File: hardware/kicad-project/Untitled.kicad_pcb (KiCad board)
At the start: 2 copper layers, 110 x 70 mm, 75 parts, among them CN2 ST-0322D00-071-1A2H, J8 Conn_01x50, Q1 DMG2301L-7, Q2 DMG2301L-7, Q3 DMG2301L-7, SW1 TS-1187A-B-A-B, SW10 TS-1135-C, SW2 TS-1187A-B-A-B, SW4 K2-1109SP-C4SA, SW5 K2-1109SP-C4SA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

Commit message: wip
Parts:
- removed R1, R11: 0, Resistor_SMD:R_0603_1608Metric
- added JP1: Gain jumper, Jumper:SolderJumper-2_P1.3mm_Open_Pad1.0x1.5mm, F.Cu at (95.7, 89.0)
- added JP2: Power jumper, Jumper:SolderJumper-2_P1.3mm_Open_Pad1.0x1.5mm, F.Cu at (140.7, 92.0)
- added TP1: Test OUTP, Connector_PinHeader_2.54mm:PinHeader_1x01_P2.54mm_Vertical, F.Cu at (108.6, 125.0)
- added TP2: Test OUTN, Connector_PinHeader_2.54mm:PinHeader_1x01_P2.54mm_Vertical, F.Cu at (105.0, 125.0)
- moved C15 0.18 mm to (185.1, 62.0)
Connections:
- C15 pad 1: Net-(Card1-VDD) -> GND
- Card1 pad 4: Net-(Card1-VDD) -> CONTROLLED_3.3V
- U1 pad 28: unconnected-(U1-IO35-Pad28) -> LCD_MOSI
- U1 pad 29: SD_DAT_1 -> LCD_DC
- U1 pad 30: SD_DAT_0 -> LCD_SCK
- U1 pad 31: SD_CLK -> LCD_CS
- U1 pad 32: SD_CMD -> SD_DAT_1
- U1 pad 33: SD_DAT_3 -> SD_DAT_0
- U1 pad 34: SD_DAT_2 -> SD_CLK
- U1 pad 35: unconnected-(U1-IO42-Pad35) -> SD_CMD
- U1 pad 38: unconnected-(U1-IO2-Pad38) -> SD_DAT_3
- U1 pad 39: unconnected-(U1-IO1-Pad39) -> SD_DAT_2
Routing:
- net LCD_CS: track 0.00 -> 55.0 mm, vias 0 -> 2
- net LCD_SCK: track 0.00 -> 53.9 mm, vias 0 -> 2
- net LCD_DC: track 0.00 -> 52.8 mm, vias 0 -> 2
- net LCD_MOSI: track 0.00 -> 51.7 mm, vias 0 -> 2
- net Net-(Card1-VDD): track 7.69 -> 0.00 mm
- net SD_DAT_3: track 94.2 -> 100.7 mm
- net SD_DAT_2: track 95.2 -> 101.4 mm
- net Net-(U6-OUTP): track 21.4 -> 26.8 mm
- net CONTROLLED_3.3V: track 187.5 -> 192.8 mm
- net +3.3V: track 149.5 -> 154.4 mm
- net SD_CLK: track 85.6 -> 90.3 mm
- net SD_CMD: track 89.2 -> 93.5 mm
- net SD_DAT_1: track 79.8 -> 83.8 mm
- net SD_DAT_0: track 80.3 -> 84.1 mm
- net GAIN_CONTROL: track 60.4 -> 57.0 mm, vias 4 -> 3
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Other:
- board text removed: "BETA"

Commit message: update MAX sdmode to 634k R
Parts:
- R8: value 1M -> 634k
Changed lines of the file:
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@@
         (effects (font (size 1 1) (thickness 0.15)))
     )
-    (fp_text value "1M" (at 3 6.43 90) (layer "F.Fab")
+    (fp_text value "634k" (at 3 6.43 90) (layer "F.Fab")
         (effects (font (size 1 1) (thickness 0.15)))
     )
@@
   (gr_circle (center 119.797921 117.336565) (end 128.297921 117.336565)
     (stroke (width 0.1) (type dash)) (fill none) (layer "F.SilkS"))
+  (gr_rect (start 139 91) (end 147 94)
+    (stroke (width 0.1524) (type default)) (fill none) (layer "F.SilkS"))
   (gr_line (start 134.313025 126.403429) (end 134.313025 105.55587)
     (stroke (width 0.2) (type solid)) (layer "Edge.Cuts"))

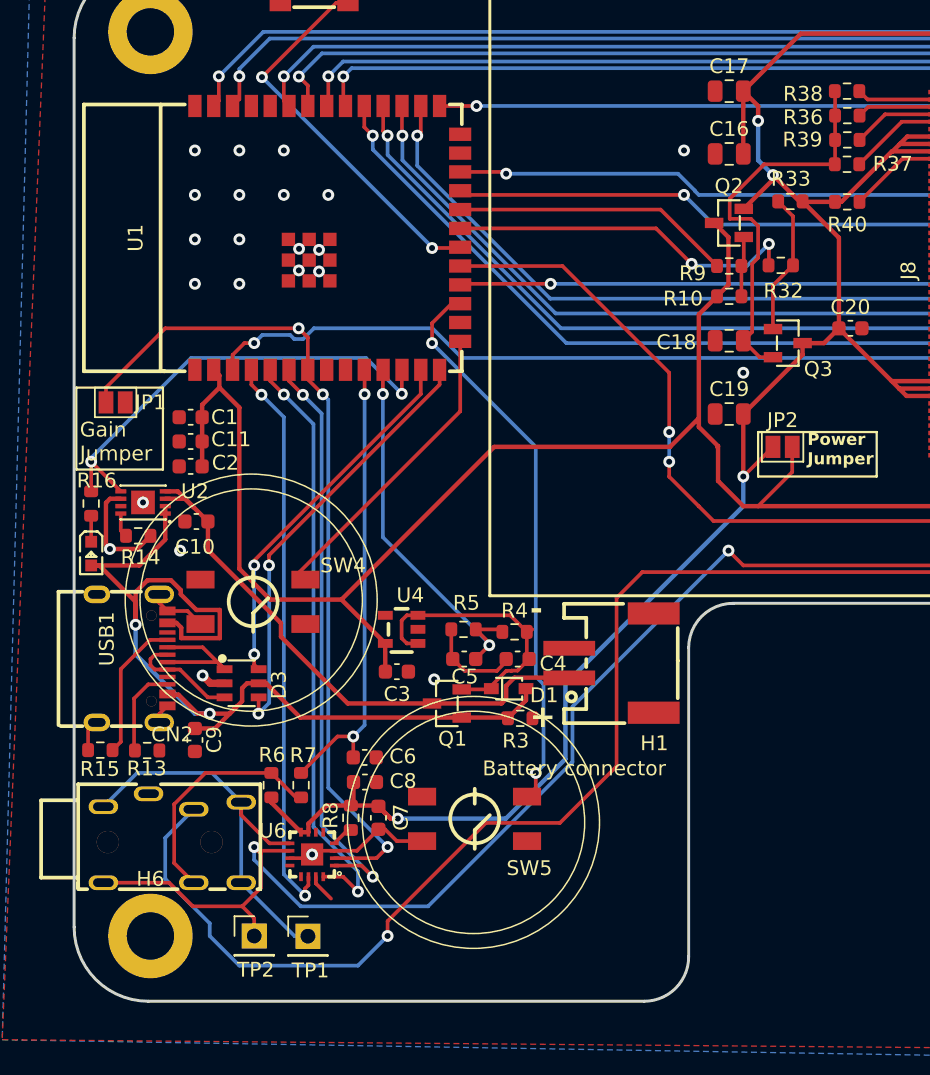
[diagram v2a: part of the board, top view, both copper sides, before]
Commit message: fix mosfet
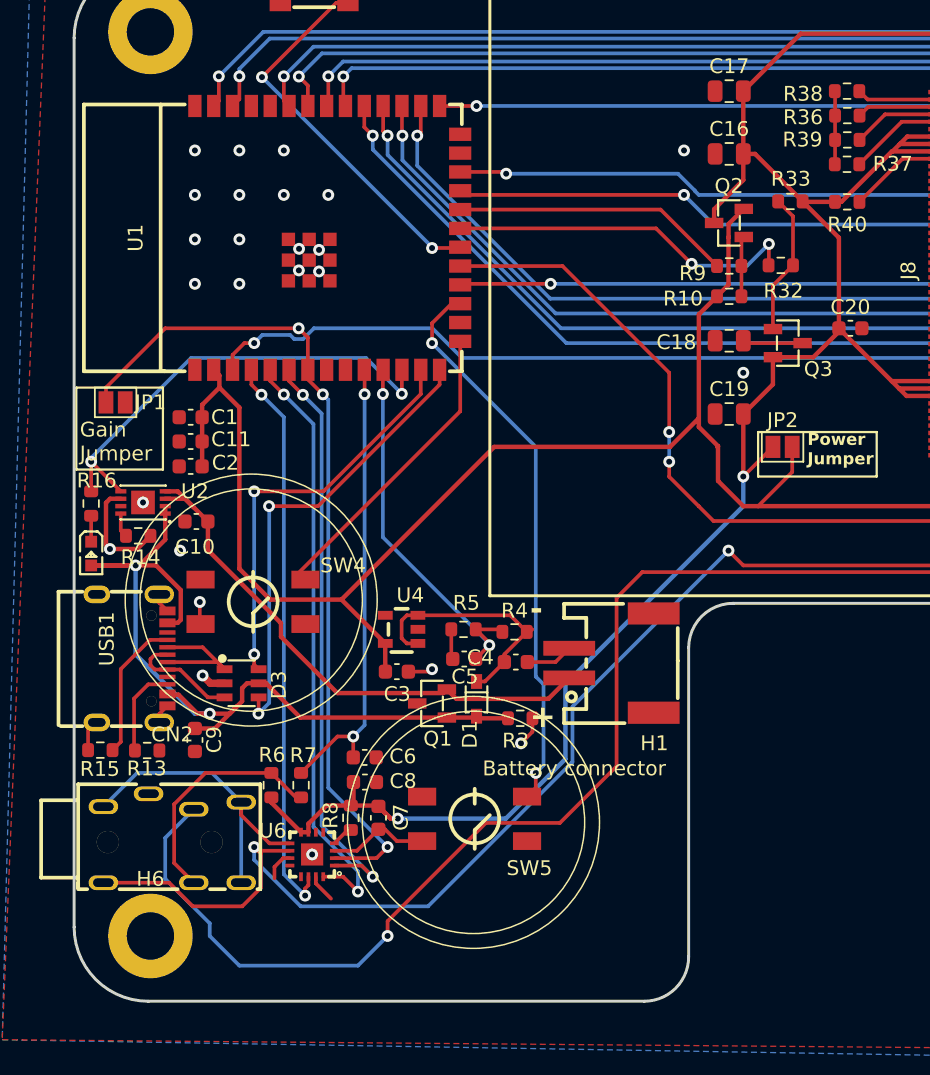
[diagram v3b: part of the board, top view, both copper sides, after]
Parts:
- removed TP1: Test OUTP, Connector_PinHeader_2.54mm:PinHeader_1x01_P2.54mm_Vertical
- removed TP2: Test OUTN, Connector_PinHeader_2.54mm:PinHeader_1x01_P2.54mm_Vertical
- moved D1 2.28 mm to (120.0, 109.0), turned to -90 degrees
- moved Q1 1.00 mm to (117.0, 109.3)
- moved C4 0.24 mm to (122.7, 106.5), turned to 180 degrees
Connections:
- C18 pad 2: Net-(Q3-S) -> Net-(Q3-D)
- Q1 pad 2: Net-(D1-K) -> +BATT
- Q1 pad 3: +BATT -> Net-(D1-K)
- Q2 pad 2: CONTROLLED_3.3V -> +3.3V
- Q2 pad 3: +3.3V -> CONTROLLED_3.3V
- Q3 pad 2: Net-(Q3-S) -> CONTROLLED_3.3V
- Q3 pad 3: CONTROLLED_3.3V -> Net-(Q3-D)
- R36 pad 2: Net-(Q3-S) -> Net-(Q3-D)
- R37 pad 2: Net-(Q3-S) -> Net-(Q3-D)
- R38 pad 2: Net-(Q3-S) -> Net-(Q3-D)
- R39 pad 2: Net-(Q3-S) -> Net-(Q3-D)
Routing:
- net Net-(Q3-S): track 27.1 -> 0.00 mm
- net +5V: track 70.3 -> 60.2 mm
- net Net-(Q3-D): track 0.00 -> 9.01 mm
- net Net-(U6-OUTP): track 26.8 -> 21.4 mm
- net GPIO_19: track 25.0 -> 27.7 mm
- net Net-(D1-K): track 19.1 -> 16.7 mm
- net Net-(U6-OUTN): track 101.3 -> 99.0 mm
- net GPIO_20: track 29.4 -> 31.3 mm
- net +3.3V: track 154.4 -> 155.4 mm
- net GND: track 62.0 -> 62.8 mm, vias 23 -> 25
- net CONTROLLED_3.3V: track 192.8 -> 192.0 mm, vias 4 -> 2
- net +BATT: track 38.4 -> 37.7 mm

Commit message: wip
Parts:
- moved H1 37.6 mm to (166.7, 107.0), turned to -90 degrees
- moved H2 37.4 mm to (129.2, 107.3), turned to 90 degrees
- moved R13 5.78 mm to (103.0, 110.0)
- moved C7 5.62 mm to (116.0, 122.0)
- moved R8 5.19 mm to (113.0, 122.0)
- moved C6 4.80 mm to (107.8, 114.0)
- moved C3 4.11 mm to (112.0, 104.0)
- moved U4 3.79 mm to (113.1, 101.0)
- moved R6 3.69 mm to (109.0, 117.2)
- moved C8 3.43 mm to (113.0, 118.0)
- moved C20 3.16 mm to (146.2, 87.0)
- moved Q3 3.16 mm to (144.0, 84.0)
- moved R9 2.88 mm to (134.2, 79.8)
- moved D3 2.85 mm to (107.0, 108.0)
- moved R7 2.62 mm to (107.0, 117.2)
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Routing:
- net Net-(CN2-Pad5): track 101.7 -> 30.3 mm, vias 1 -> 0
- net +BATT: track 37.7 -> 90.9 mm, vias 0 -> 2
- net Net-(U6-OUTN): track 99.0 -> 53.3 mm, vias 2 -> 0
- net GND: track 62.8 -> 32.0 mm, vias 25 -> 52
- net Net-(Q3-D): track 9.01 -> 28.8 mm, vias 0 -> 2
- net +5V: track 60.2 -> 41.9 mm, vias 2 -> 0
- net +3.3V: track 155.4 -> 140.3 mm, vias 0 -> 4
- net BTN_4: track 82.2 -> 91.6 mm
- net EN: track 123.9 -> 132.7 mm
- net BTN_5: track 26.1 -> 33.2 mm
- net BOOT: track 106.2 -> 112.5 mm
- net CONTROLLED_3.3V: track 192.0 -> 198.1 mm, vias 2 -> 8
- net LCD_CS: track 55.0 -> 61.0 mm
- net Net-(CN2-Pad6): track 16.0 -> 10.2 mm
- net I2S_DOUT: track 39.4 -> 44.6 mm
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
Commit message: wip
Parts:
- moved C7 7.73 mm to (109.7, 117.5), turned to 180 degrees
- moved C4 6.94 mm to (116.3, 102.0), turned to 90 degrees
- moved R6 4.37 mm to (112.0, 114.0), turned to 180 degrees
- moved C8 3.38 mm to (109.8, 119.0)
- moved C3 0.93 mm to (112.7, 103.4)
- moved C5 0.83 mm to (118.8, 105.0)
- moved R4 0.83 mm to (122.8, 104.0)
- moved R5 0.83 mm to (118.8, 102.0)
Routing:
- net Net-(CN2-Pad6): track 10.2 -> 13.4 mm
- net GND: track 32.0 -> 30.5 mm
- net Net-(D1-K): track 18.9 -> 17.8 mm
- net CONTROLLED_3.3V: track 198.1 -> 199.0 mm
- net +3.3V: track 140.3 -> 139.4 mm
- net BAT_READ: track 23.2 -> 24.0 mm

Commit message: wip
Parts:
- removed R36, R37, R38, R39: 10, Resistor_SMD:R_0603_1608Metric
- removed U4: XC6220B331MR, easyeda2kicad:SOT-23-5_L2.9-W1.6-P0.95-LS2.8-BR
- added C12: 10uf, Capacitor_SMD:C_0603_1608Metric, F.Cu at (110.7, 98.3)
- added R1: 10, Resistor_SMD:R_0603_1608Metric, F.Cu at (145.0, 66.0)
- added R11: 10, Resistor_SMD:R_0603_1608Metric, F.Cu at (145.0, 70.0)
- added R17: 10, Resistor_SMD:R_0603_1608Metric, F.Cu at (145.0, 72.0)
- added R2: 10, Resistor_SMD:R_0603_1608Metric, F.Cu at (145.0, 68.0)
- added U3: ME6217C33P5G, easyeda2kicad:SOT-89-5_L4.5-W2.5-P1.50-LS4.5-BR, F.Cu at (113.5, 101.3)
- C4: value 10uF -> 10uf
- moved C5 16.4 mm to (112.9, 89.7)
- moved C3 6.82 mm to (117.9, 99.0), turned to -90 degrees
- moved C4 3.09 mm to (116.3, 98.9), turned to -90 degrees
- moved R5 2.00 mm to (118.8, 104.0)
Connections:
- net /random/LCD_NRST renamed Net-(J8-Pin_10)
- C18 pad 2: Net-(Q3-D) -> Net-(J8-Pin_1)
- C3 pad 1: +3.3V -> GND
- C3 pad 2: GND -> Net-(D1-K)
- J8 pad 1: GND -> Net-(J8-Pin_1)
- J8 pad 7: CONTROLLED_3.3V -> +3.3V
- J8 pad 8: CONTROLLED_3.3V -> +3.3V
- J8 pad 9: CONTROLLED_3.3V -> +3.3V
- Q3 pad 2: CONTROLLED_3.3V -> +3.3V
- Q3 pad 3: Net-(Q3-D) -> Net-(J8-Pin_1)
- R33 pad 2: CONTROLLED_3.3V -> +3.3V
- R40 pad 1: CONTROLLED_3.3V -> +3.3V
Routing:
- net Net-(Q3-D): track 28.8 -> 0.00 mm, vias 2 -> 0
- net Net-(D1-K): track 17.8 -> 34.2 mm
- net Net-(J8-Pin_1): track 0.00 -> 10.4 mm, vias 0 -> 2
- net GPIO_20: track 27.8 -> 32.2 mm
- net +3.3V: track 139.4 -> 136.4 mm
- net BAT_READ: track 24.0 -> 22.0 mm
- net GND: track 30.5 -> 29.9 mm, vias 52 -> 28
- net +BATT: track 90.9 -> 91.6 mm

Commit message: wip
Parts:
- removed JP1: Gain jumper, Jumper:SolderJumper-2_P1.3mm_Open_Pad1.0x1.5mm
- removed JP2: Power jumper, Jumper:SolderJumper-2_P1.3mm_Open_Pad1.0x1.5mm
- removed Q2: DMG2301L-7, easyeda2kicad:SOT-23-3_L2.9-W1.3-P1.90-LS2.4-BR
- removed R10: 100k, Resistor_SMD:R_0603_1608Metric
- removed R8: 634k, Resistor_SMD:R_0603_1608Metric
- removed R9: 330, Resistor_SMD:R_0603_1608Metric
- moved C9 37.2 mm to (136.0, 97.0)
- moved U2 34.5 mm to (132.0, 96.0)
- moved R16 34.0 mm to (128.0, 96.0)
- moved R14 33.8 mm to (131.0, 98.0)
- moved C10 33.1 mm to (136.0, 95.0), turned to 0 degrees
- moved C6 24.9 mm to (112.5, 89.6), turned to 90 degrees
- moved C17 22.8 mm to (143.0, 90.0), turned to 90 degrees
- moved C18 21.8 mm to (146.0, 66.0), turned to 180 degrees
- moved C16 19.5 mm to (145.0, 90.0), turned to 90 degrees
- moved R3 16.0 mm to (116.0, 93.8)
- moved R15 13.5 mm to (108.0, 107.0), turned to 0 degrees
- moved D1 13.0 mm to (119.0, 96.0), turned to 180 degrees
- moved Q1 12.5 mm to (122.0, 99.0)
- moved C19 12.0 mm to (147.0, 90.0), turned to 90 degrees
- moved R5 12.0 mm to (119.2, 92.0)
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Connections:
- C15 pad 2: CONTROLLED_3.3V -> +3.3V
- C16 pad 2: CONTROLLED_3.3V -> +3.3V
- C17 pad 2: CONTROLLED_3.3V -> +3.3V
- C19 pad 2: CONTROLLED_3.3V -> +3.3V
- C20 pad 1: CONTROLLED_3.3V -> +3.3V
- C7 pad 2: CONTROLLED_3.3V -> +3.3V
- C8 pad 2: CONTROLLED_3.3V -> +3.3V
- Card1 pad 4: CONTROLLED_3.3V -> +3.3V
- J8 pad 40: CONTROLLED_3.3V -> +3.3V
- J8 pad 41: CONTROLLED_3.3V -> +3.3V
- J8 pad 42: CONTROLLED_3.3V -> +3.3V
- R26 pad 2: CONTROLLED_3.3V -> +3.3V
- R27 pad 2: CONTROLLED_3.3V -> +3.3V
- R28 pad 2: CONTROLLED_3.3V -> +3.3V
- R29 pad 2: CONTROLLED_3.3V -> +3.3V
- R30 pad 2: CONTROLLED_3.3V -> +3.3V
- R31 pad 2: CONTROLLED_3.3V -> +3.3V
- R6 pad 1: CONTROLLED_3.3V -> +3.3V
- U1 pad 22: PERIPH_EN -> unconnected-(U1-IO14-Pad22)
- U1 pad 8: unconnected-(U1-IO15-Pad8) -> AMP_EN
- U6 pad 4: Net-(U6-~{SD_MODE}) -> AMP_EN
- U6 pad 7: CONTROLLED_3.3V -> +3.3V
- U6 pad 8: CONTROLLED_3.3V -> +3.3V
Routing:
- net CONTROLLED_3.3V: track 199.0 -> 0.00 mm, vias 8 -> 0
- net EN: track 132.7 -> 0.00 mm, vias 2 -> 0
- net BOOT: track 112.5 -> 0.00 mm, vias 2 -> 0
- net SD_DAT_2: track 98.6 -> 0.00 mm, vias 2 -> 0
- net SD_DAT_3: track 95.7 -> 0.00 mm, vias 2 -> 0
- net BTN_7: track 91.9 -> 0.00 mm, vias 2 -> 0
- net BTN_4: track 91.6 -> 0.00 mm, vias 2 -> 0
- net SD_CMD: track 89.0 -> 0.00 mm, vias 2 -> 0
- net +3.3V: track 136.4 -> 48.1 mm, vias 4 -> 0
- net BTN_3: track 88.0 -> 0.00 mm, vias 2 -> 0
- net +BATT: track 91.6 -> 3.86 mm, vias 2 -> 0
- net SD_CLK: track 87.6 -> 0.00 mm, vias 3 -> 0
- net SD_DAT_0: track 82.6 -> 0.00 mm, vias 2 -> 0
- net BTN_6: track 81.4 -> 0.00 mm, vias 2 -> 0
- net SD_DAT_1: track 79.5 -> 0.00 mm, vias 2 -> 0
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
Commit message: routing
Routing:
- net +3.3V: track 48.1 -> 250.7 mm, vias 0 -> 2
- net EN: track 0.00 -> 131.9 mm, vias 0 -> 2
- net BOOT: track 0.00 -> 114.3 mm, vias 0 -> 2
- net BTN_3: track 0.00 -> 99.3 mm, vias 0 -> 2
- net BTN_4: track 0.00 -> 98.9 mm, vias 0 -> 2
- net SD_DAT_2: track 0.00 -> 98.3 mm, vias 0 -> 2
- net SD_DAT_3: track 0.00 -> 95.6 mm, vias 0 -> 2
- net BTN_7: track 0.00 -> 94.8 mm, vias 0 -> 2
- net SD_CMD: track 0.00 -> 90.6 mm, vias 0 -> 2
- net SD_CLK: track 0.00 -> 87.3 mm, vias 0 -> 2
- net SD_DAT_0: track 0.00 -> 83.5 mm, vias 0 -> 2
- net BTN_6: track 0.00 -> 82.6 mm, vias 0 -> 2
- net SD_DAT_1: track 0.00 -> 80.3 mm, vias 0 -> 2
- net Net-(U6-OUTN): track 0.00 -> 55.5 mm
- net +BATT: track 3.86 -> 59.3 mm, vias 0 -> 4
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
